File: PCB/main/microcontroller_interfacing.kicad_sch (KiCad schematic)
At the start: 10 parts, among them J5 USB_B_Micro, U6 CAT24C256, U7 CP2102-GMR

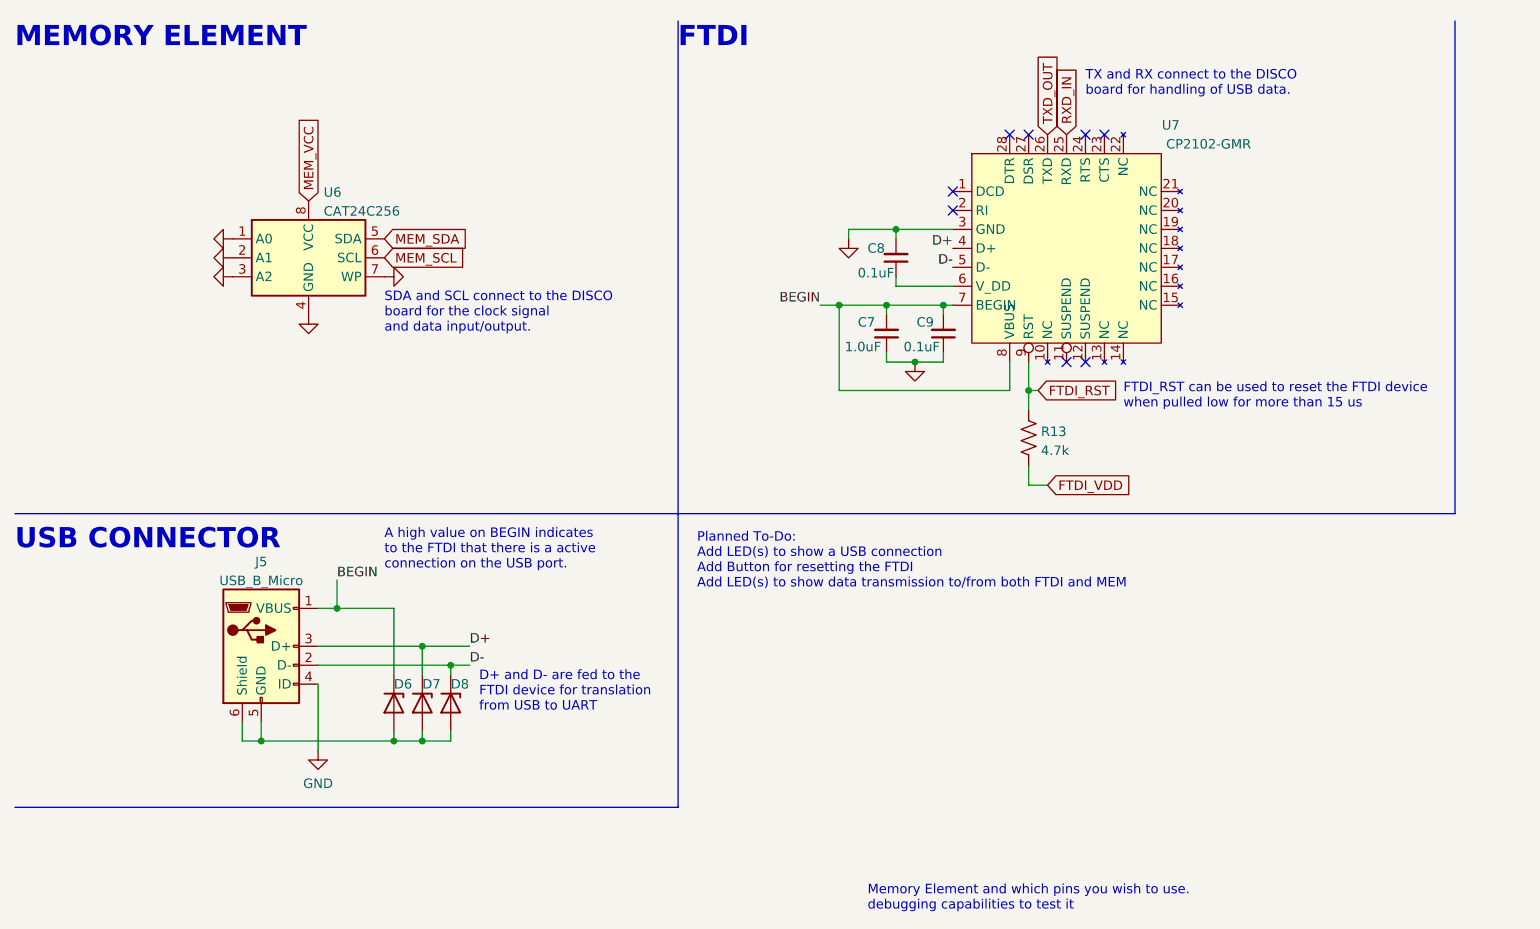
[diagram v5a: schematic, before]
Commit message: Fiddled a bit with labels
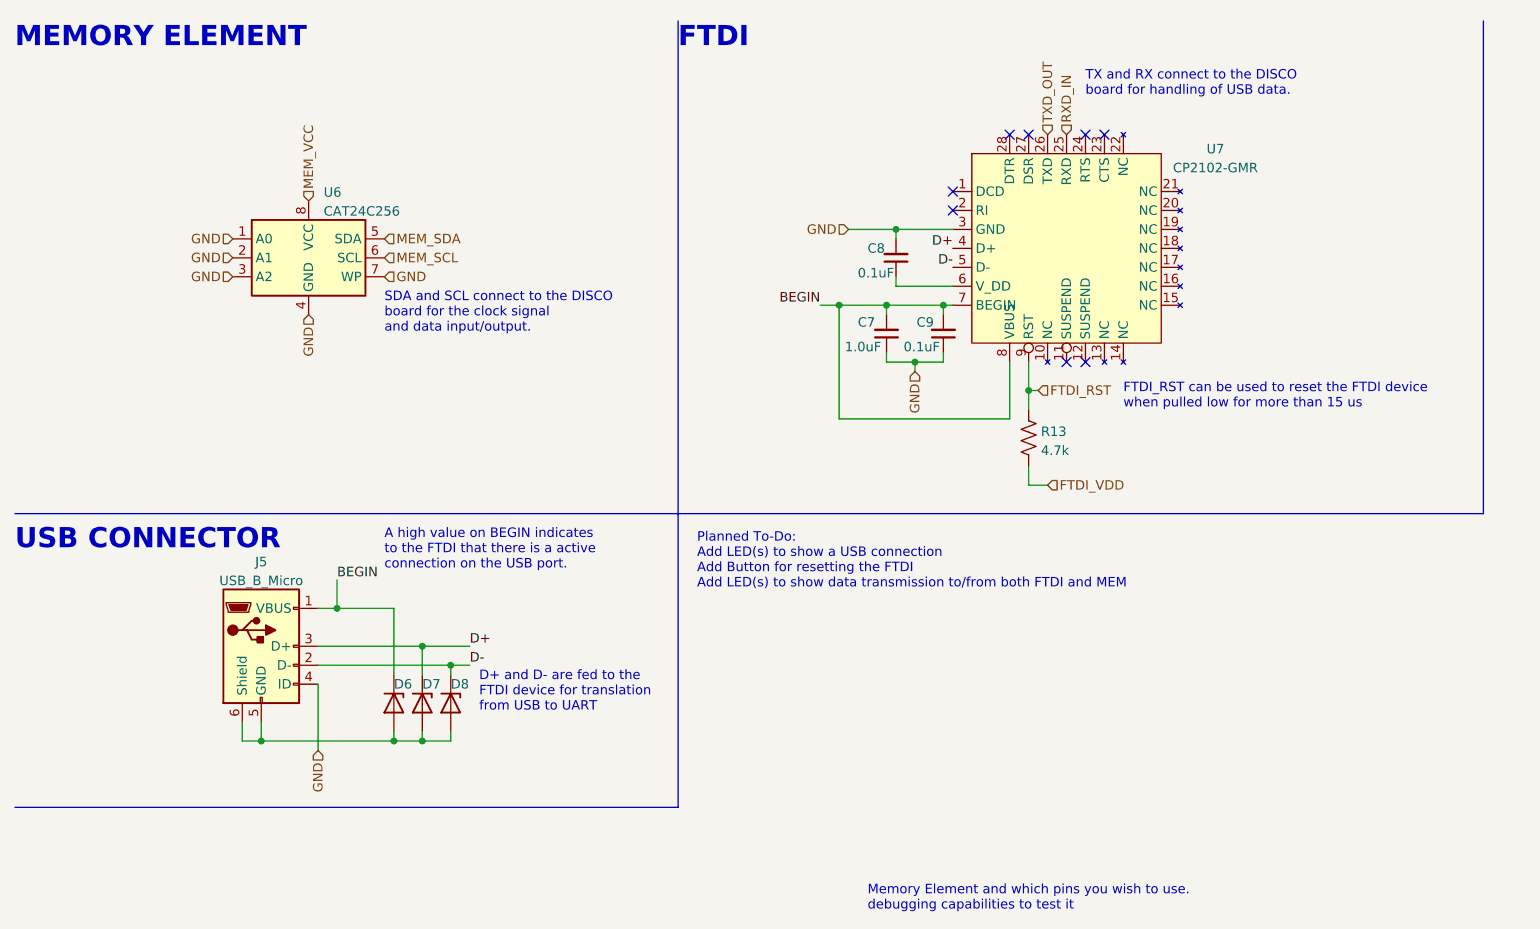
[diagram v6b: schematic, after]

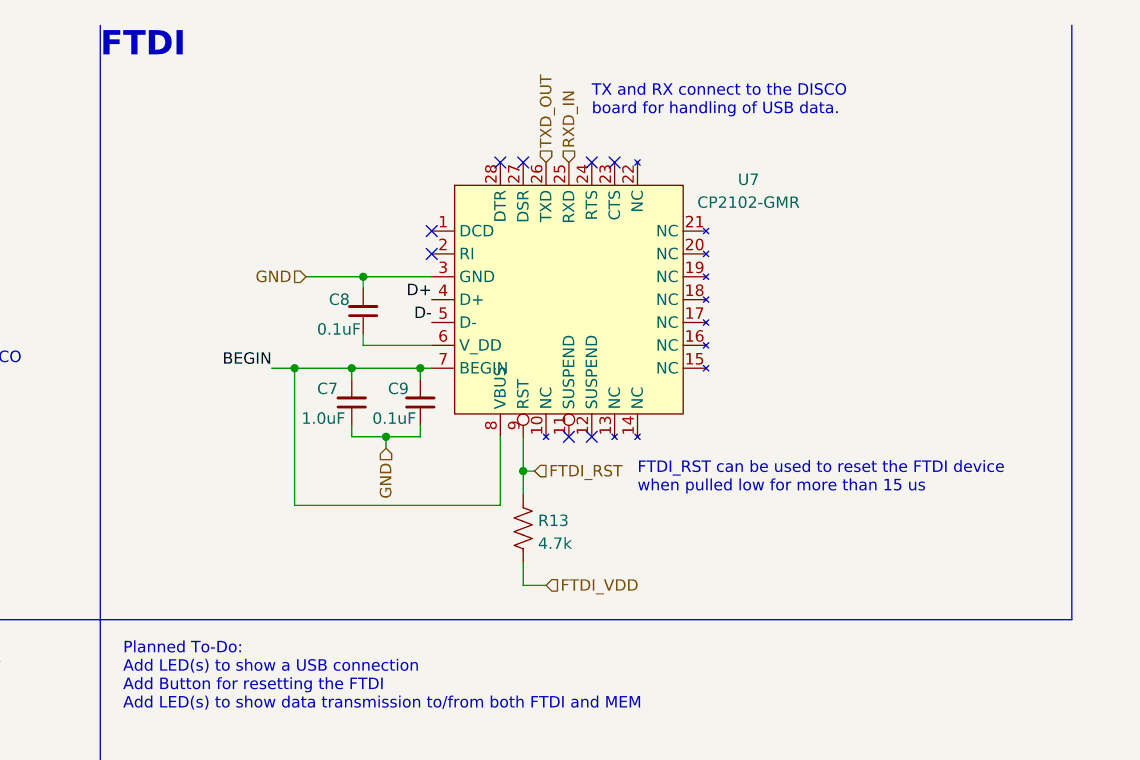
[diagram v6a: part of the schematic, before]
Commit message: Added Footprint and symbol files
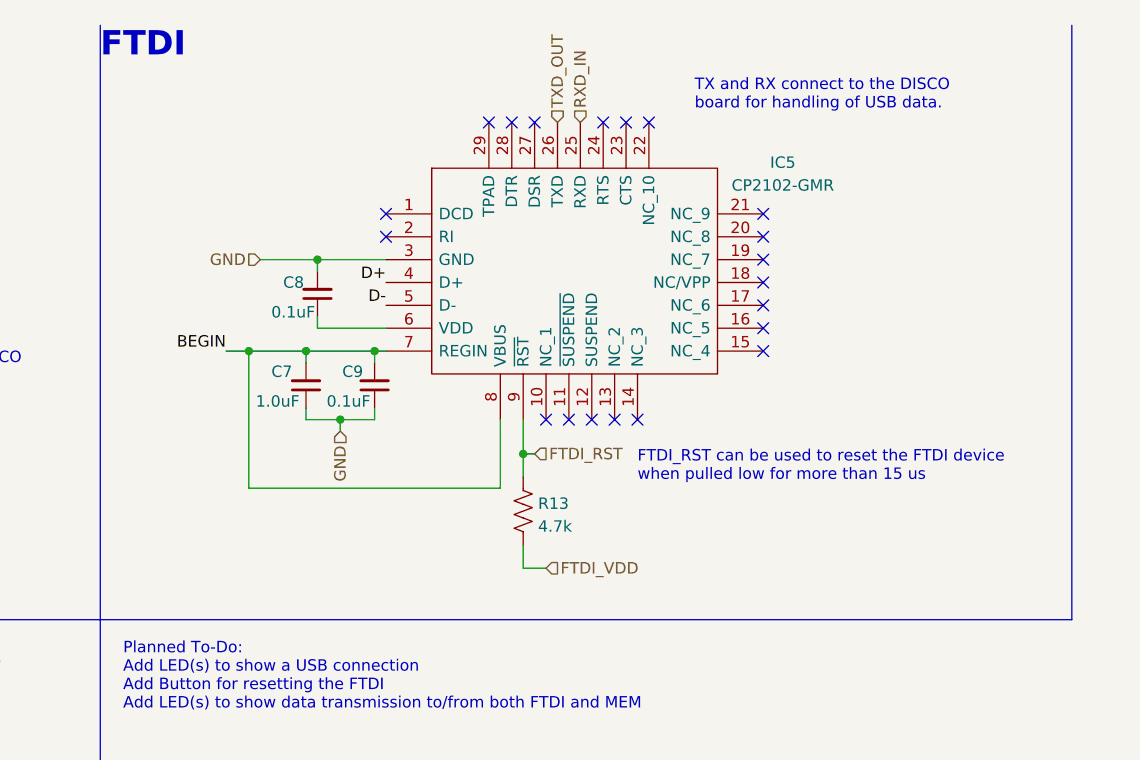
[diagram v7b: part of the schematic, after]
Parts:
- removed U7: CP2102-GMR, symbol custom_symbols:CP2102-GMR
- added IC5: CP2102-GMR, symbol CP2102-GMR:CP2102-GMR
- R13: footprint (none) -> Resistor_SMD:R_0805_2012Metric
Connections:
- net BEGIN: now also IC5.7 (REGIN), IC5.8 (VBUS)
- net D+: now also IC5.4 (D+)
- net D-: now also IC5.5 (D-)
- net FTDI_RST: now also IC5.9 (~{RST})
- net GND: now also IC5.3 (GND)
- net RXD_IN: now also IC5.25 (RXD)
- net TXD_OUT: now also IC5.26 (TXD)
- net at C8.1: now also IC5.6 (VDD)
- no-connect marks 8 -> 20
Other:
- moved on the sheet: C7, C8, C9, R13
